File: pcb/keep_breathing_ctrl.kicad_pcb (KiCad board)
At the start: 4 copper layers, 112 x 131 mm, 177 parts, among them J2 Screw_Terminal, P1 CONN_RASPBERRY, Q1 PN2222, Q2 PN2222, U1 MPL3115A2, U10 PCF8523TK, U11 AQH3213AX, U12 AQH3213AX, U13 HTS221, U14 ICE40UP5K-SG48ITR, U15 GD25Q32CTIGR-Memory_Flash, U16 UCC12040, U17 ISO7762, U18 ZLDO1117G33TA, U19 NCP177, U2 powerSTEP01, U3 TLP240D, U4 TLP240D, U5 TLP240D, U6 TLP240D, U7 TLP240D, U8 TLP240D, U9 ZLDO1117G33TA, Y1 ABS06-107-32.768KHZ-T

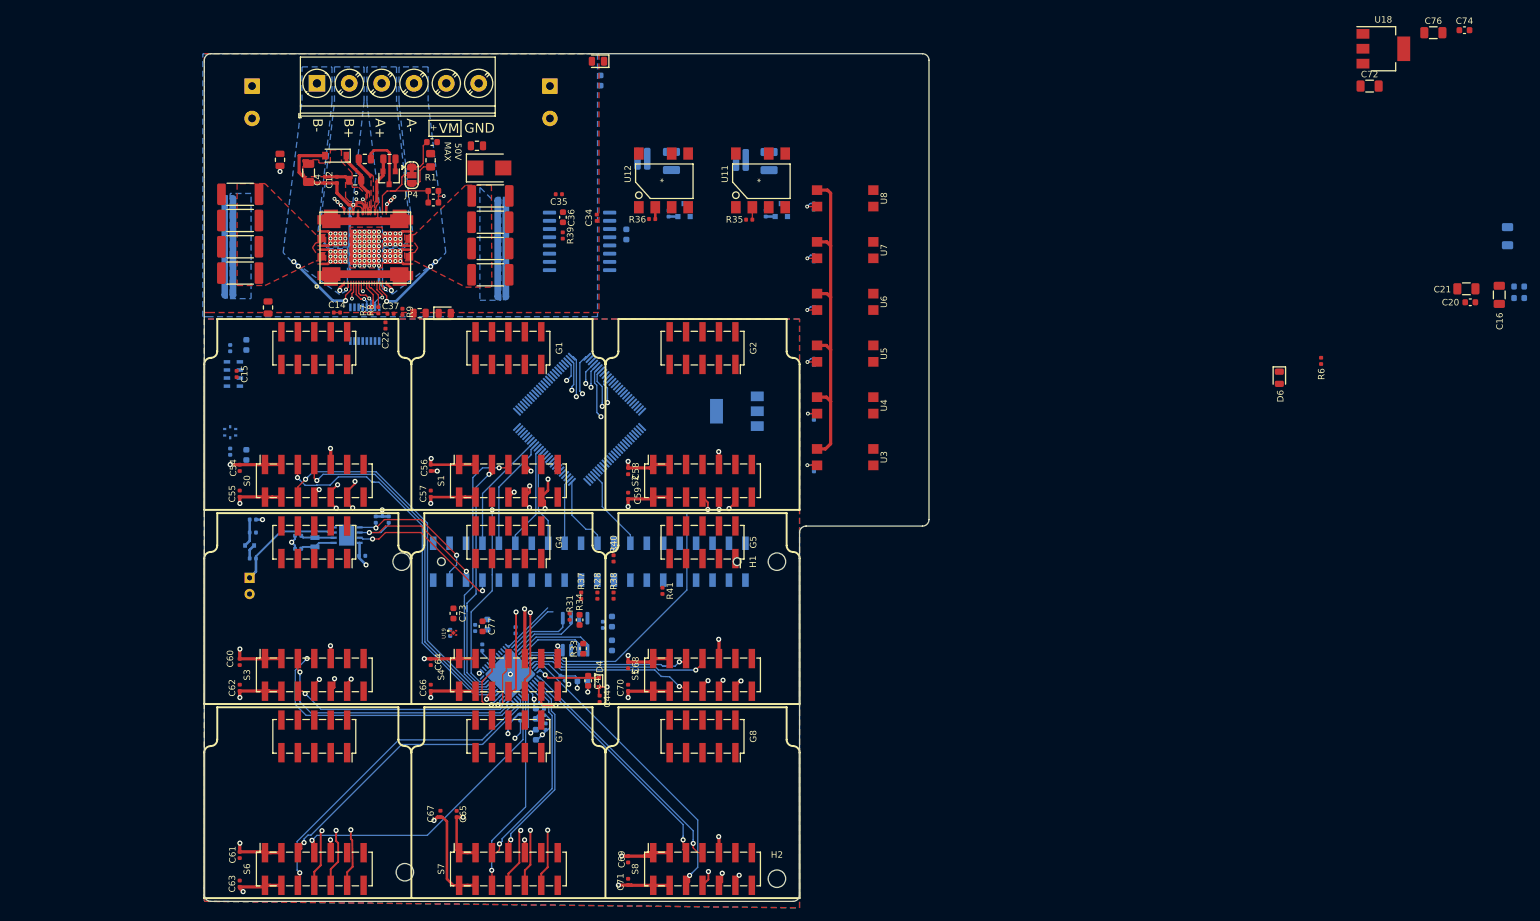
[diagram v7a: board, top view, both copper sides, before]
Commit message: fixing RPi mounting holes
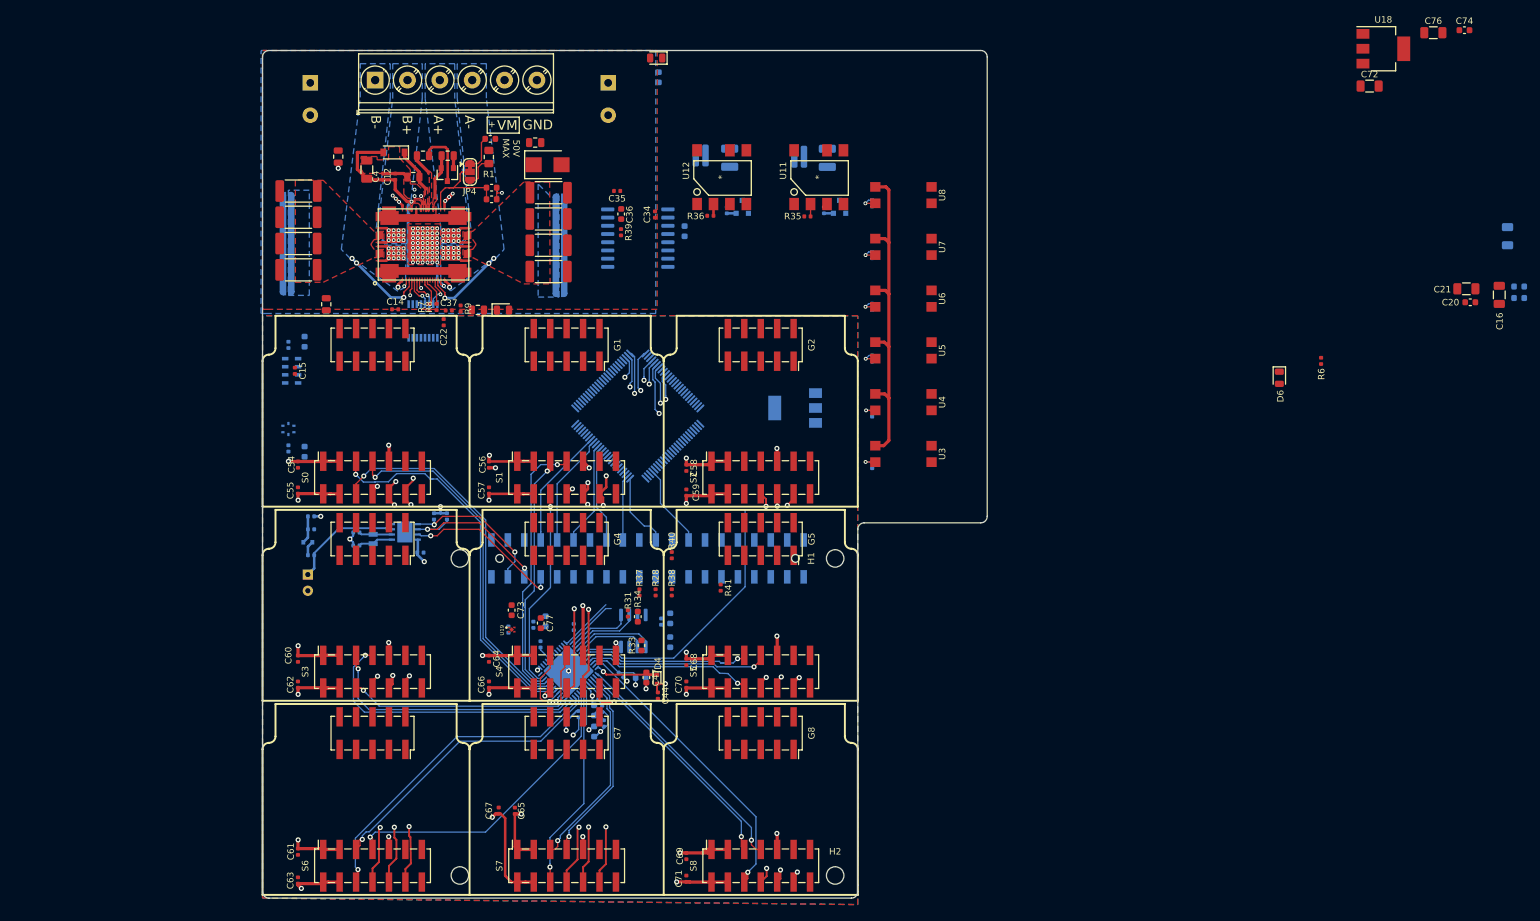
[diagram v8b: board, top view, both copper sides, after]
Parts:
- moved C35 9.01 mm to (133.3, 47.7)
- moved R31 9.01 mm to (135.0, 113.0)
- moved C1 9.01 mm to (94.6, 44.4)
- moved C10 9.01 mm to (85.9, 31.0)
- moved C12 9.01 mm to (99.0, 45.5)
- moved C13 9.01 mm to (103.3, 42.3)
- moved C14 9.01 mm to (99.0, 66.0)
- moved C15 9.01 mm to (83.5, 75.5)
- moved C2 9.01 mm to (101.8, 45.6)
- moved C22 9.01 mm to (106.5, 68.0)
- moved C23 9.01 mm to (93.0, 100.5)
- moved C24 9.01 mm to (85.5, 107.0)
- moved C25 9.01 mm to (93.0, 102.5)
- moved C26 9.01 mm to (102.9, 103.6)
- moved C27 9.01 mm to (165.8, 42.6)
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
